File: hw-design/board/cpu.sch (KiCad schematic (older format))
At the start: 15 parts, among them P1 CONN_02X05, P2 CONN_02X05, U4 LPC1113FBD48/302, X1 10MHz

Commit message: sch: cpu reset done (wip)
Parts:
- removed R27, R28: 100R, Resistors_SMD:R_0603, symbol R
- added C? (x2): C, symbol C
- added C? (x3): 100nF X7R, Capacitors_SMD:C_0603, symbol C
- added C?: 10nF 500V, symbol C
- added C?: 10nF, symbol C
- added P?: USB_OTG, symbol USB_OTG
- added P?: CONN_01X04, symbol CONN_01X04
- added Q?: BC857, symbol Q_PNP_BEC
- added R? (x2): 33R, symbol R
- added R?: 100R, symbol R
- added R?: 1M, symbol R
- added R? (x2): 3k, symbol R
- added R?: 24k, symbol R
- added R? (x5): 10k, symbol R
- added SW?: SW_PUSH, symbol SW_PUSH
- added U?: LPC11U24FBD48/401, Housings_QFP:LQFP-80_12x12mm_Pitch0.5mm, symbol LPC11U24FBD48/401
- added Y?: 10MHz, symbol Crystal_Small
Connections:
- net +3V3: now also C?.2, C?.2, Q?.2 (E), R?.1, R?.1, R?.1, R?.1, R?.1, R?.2, U?.44 (VDD), U?.8 (VDD); no longer P2.1 (P1)
- net GNDD: now also C?.1, C?.1, C?.1, C?.2, C?.2, C?.2, C?.2, P?.1 (P1), P?.5 (GND), R?.1, SW?.2, U?.41 (VSS), U?.5 (VSS); no longer P2.7 (P7)
- net RESET: now also C?.2, R?.2, SW?.1, U?.3 (~RESET~/PIO0_0)
- net TCK_SWDCLK: now reaches P2.4 (P4)
- net TCK_SWDCLK: now also R?.2, U?.29 (SWCLK/PIO0_10/SCK0/CT16B0_MAT2)
- net TMS_SDWIO: now reaches P2.2 (P2)
- net TMS_SDWIO: now also R?.2, U?.33 (TMS/PIO0_12/AD1/CT32B1_CAP0)
- net TDO_SWO: now reaches P2.6 (P6)
- net TDO_SWO: now also R?.2, U?.34 (TDO/PIO0_13/AD2/CT32B1_MAT0)
- net TDI: now reaches P2.8 (P8)
- net TDI: now also R?.2, U?.32 (TDI/PIO0_11/AD0/CT32B0_MAT3)
- new net: C?.1, U?.6 (XTALIN), Y?.1
- new net: C?.1, U?.7 (XTALOUT), Y?.2
- new net: P?.2 (D-), R?.2
- new net: P?.3 (D+), R?.1, R?.2
- new net: C?.1, P?.6 (shield), R?.2
- new net: Q?.1 (B), R?.1, R?.2
- new net: Q?.3 (C), R?.2
- new net CHAIN_DE: P?.4 (P4), U?.43 (PIO1_15/~DCD~/CT16B0_MAT2/SCK1)
- new net CHAIN_RX: P?.3 (P3), U?.37 (PIO1_14/~DSR~/CT16B0_MAT1/RXD)
- new net CHAIN_TX: P?.2 (P2), U?.36 (PIO1_13/~DTR~/CT16B0_MAT0/TXD)
- new net USB_CONNECT: R?.1, U?.22 (PIO0_6/~USB_CONNECT~/SCK0)
- new net USB_DM: R?.1, U?.19 (USB_DM)
- new net USB_DP: R?.1, U?.20 (USB_DP)
- new net USB_VBUS: R?.1, U?.14 (PIO0_3/USB_VBUS)
- new net VCC: C?.1, P?.1 (VCC), R?.2
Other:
- note added: "JTAG"
- note added: "RESET"
- note added: "USB DEVICE"
- note removed: "SWD"
- moved on the sheet: C12, C13, C14, C15, C16, P1, P2, R23, R24, R25, R26, U4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

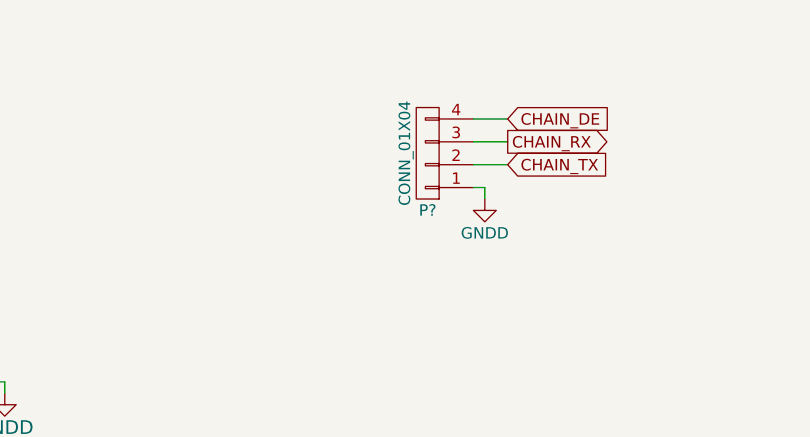
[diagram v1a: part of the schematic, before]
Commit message: sch: cpu, I/Os and control chain circuits done
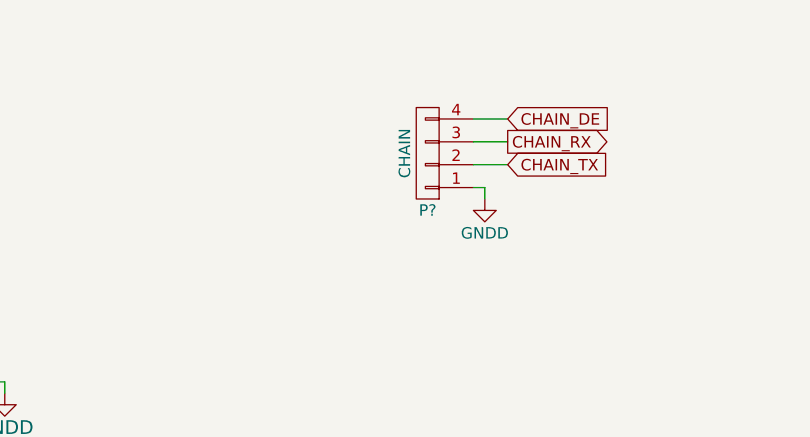
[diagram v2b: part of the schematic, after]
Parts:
- P?: value CONN_01X04 -> CHAIN
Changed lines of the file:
@@
 P 1450 1250
 F 0 "P?" H 1450 1500 50  0000 C CNN
-F 1 "CONN_01X04" V 1550 1250 50  0000 C CNN
+F 1 "CHAIN" V 1550 1250 50  0000 C CNN
 F 2 "" H 1450 1250 60  0000 C CNN
 F 3 "" H 1450 1250 60  0000 C CNN

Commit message: sch: schematic annotation done
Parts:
- removed C12, C14: 18pF X7R, Capacitors_SMD:C_0603, symbol C
- removed C13, C15, C16: 100nF X7R, Capacitors_SMD:C_0603, symbol C
- removed P1: CONN_02X05, Pin_Headers:Pin_Header_Straight_2x05, symbol CONN_02X05
- removed R23: 10k, Resistors_SMD:R_0603, symbol R
- removed R24, R25, R26: 0R, Resistors_SMD:R_0603, symbol R
- removed R? (x4): 10k, symbol R
- removed U4: LPC1113FBD48/302, Housings_QFP:LQFP-48_7x7mm_Pitch0.5mm, symbol LPC1113FBD48/302
- removed X1: 10MHz, Crystals_Oscillators_SMD:Q_49U3HMS, symbol Crystal
- gave numbers to parts that had none: 21
- renumbered P2 to P3
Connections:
- net POT: now also U4.32 (TDI/PIO0_11/AD0/CT32B0_MAT3)
- net SWDIO: now also U4.39 (SWDIO/PIO0_15/AD4/CT32B1_MAT2)
- net CH2: now reaches U4.13 (PIO1_20/~DSR~/SCK1)
- net FS1: now reaches U4.18 (PIO1_23/CT16B1_MAT1/SSEL1)
- net CH1: now reaches U4.2 (PIO1_19/~DTR~/SSEL1)
- net FS1_LED_R: now reaches U4.24 (PIO1_28/CT32B0_CAP0/SCLK)
- net FS1_LED_B: now reaches U4.25 (PIO1_31)
- net CH3: now reaches U4.26 (PIO1_21/~DCD~/MISO1)
- net SWO: now reaches U4.28 (PIO0_9/MOSI0/CT16B0_MAT1)
- net SWO: now also P3.6 (P6)
- net FS1_LED_G: now reaches U4.31 (PIO1_29/SCK0/CT32B0_CAP1)
- net RS485_RX_LED: now reaches U4.46 (PIO0_18/RXD/CT32B0_MAT0)
- net RS485_TX_LED: now reaches U4.47 (PIO0_19/TXD/CT32B0_MAT1)
- net TCK_SWDCLK renamed SWCLK
- net TDI: no longer names the net of P3.8 (P8)
- net TDI: no longer U4.32 (TDI/PIO0_11/AD0/CT32B0_MAT3)
- net TDO_SWO: no longer names the net of U4.34 (TDO/PIO0_13/AD2/CT32B1_MAT0)
- net TDO_SWO: no longer P3.6 (P6)
- net TMS_SDWIO: no longer names the net of U4.33 (TMS/PIO0_12/AD1/CT32B1_CAP0)
- net TMS_SDWIO: no longer P3.2 (P2)
- new net SDWIO: P3.2 (P2)
- no-connect marks 33 -> 24
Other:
- note added: "SWD"
- note removed: "JTAG"
- moved on the sheet: C16, P3, R21, SW1

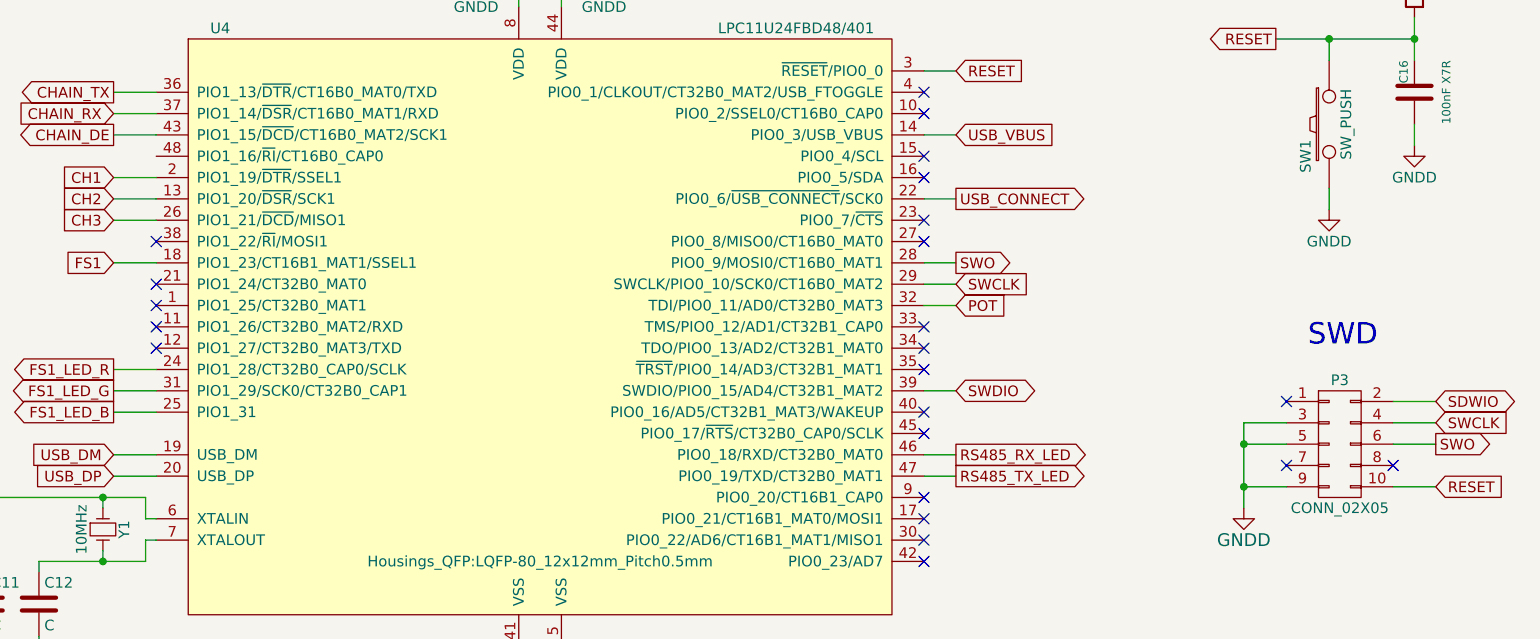
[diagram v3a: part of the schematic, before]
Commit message: sch: errors fixed, DRC passing
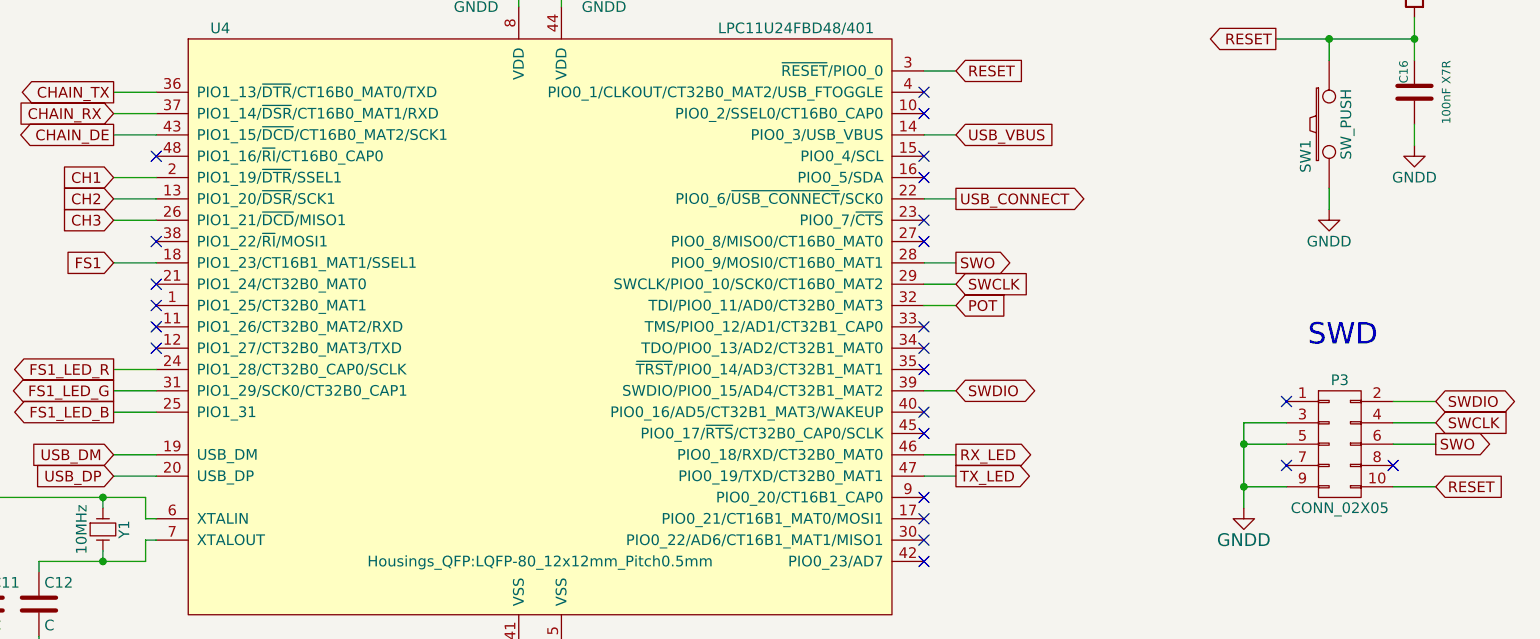
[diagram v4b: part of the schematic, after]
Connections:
- net SDWIO is gone; now on net SWDIO: P3.2 (P2)
- net RS485_RX_LED renamed RX_LED
- net RS485_TX_LED renamed TX_LED
- no-connect marks 24 -> 25
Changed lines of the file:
@@
 SWD
 $Comp
-L GNDD #PWR040
+L GNDD #PWR043
 U 1 1 54E5DFA7
 P 9200 3950
-F 0 "#PWR040" H 9200 3700 60  0001 C CNN
+F 0 "#PWR043" H 9200 3700 60  0001 C CNN
 F 1 "GNDD" H 9200 3800 60  0000 C CNN
 F 2 "" H 9200 3950 60  0000 C CNN
@@
 $EndComp
 $Comp
-L GNDD #PWR041
+L GNDD #PWR044
 U 1 1 556F6417
 P 3300 4600
-F 0 "#PWR041" H 3300 4350 50  0001 C CNN
+F 0 "#PWR044" H 3300 4350 50  0001 C CNN
 F 1 "GNDD" H 3300 4450 50  0000 C CNN
 F 2 "" H 3300 4600 60  0000 C CNN
@@
 $EndComp
 $Comp
-L GNDD #PWR042
+L GNDD #PWR045
 U 1 1 556F65EC
 P 3550 4600
-F 0 "#PWR042" H 3550 4350 50  0001 C CNN
+F 0 "#PWR045" H 3550 4350 50  0001 C CNN
 F 1 "GNDD" H 3550 4450 50  0000 C CNN
 F 2 "" H 3550 4600 60  0000 C CNN
@@
 USB_VBUS
 $Comp
-L +3.3V #PWR043
+L +3.3V #PWR046
 U 1 1 55705A80
 P 5900 850
-F 0 "#PWR043" H 5900 700 50  0001 C CNN
+F 0 "#PWR046" H 5900 700 50  0001 C CNN
 F 1 "+3.3V" H 5900 990 50  0000 C CNN
 F 2 "" H 5900 850 60  0000 C CNN
@@
 $EndComp
 $Comp
-L GNDD #PWR044
+L GNDD #PWR047
 U 1 1 557DC875
 P 5600 1450
-F 0 "#PWR044" H 5600 1200 50  0001 C CNN
+F 0 "#PWR047" H 5600 1200 50  0001 C CNN
 F 1 "GNDD" H 5600 1300 50  0000 C CNN
 F 2 "" H 5600 1450 60  0000 C CNN
@@
 $EndComp
 $Comp
-L GNDD #PWR045
+L GNDD #PWR048
 U 1 1 557DCAD9
 P 6200 1450
-F 0 "#PWR045" H 6200 1200 50  0001 C CNN
+F 0 "#PWR048" H 6200 1200 50  0001 C CNN
 F 1 "GNDD" H 6200 1300 50  0000 C CNN
 F 2 "" H 6200 1450 60  0000 C CNN
@@
 $EndComp
 $Comp
-L GNDD #PWR046
+L GNDD #PWR049
 U 1 1 557DD01E
 P 5900 4750
-F 0 "#PWR046" H 5900 4500 50  0001 C CNN
+F 0 "#PWR049" H 5900 4500 50  0001 C CNN
 F 1 "GNDD" H 5900 4600 50  0000 C CNN
 F 2 "" H 5900 4750 60  0000 C CNN
@@
 $EndComp
 $Comp
-L GNDD #PWR047
+L GNDD #PWR050
 U 1 1 557DE7E3
 P 2850 6600
-F 0 "#PWR047" H 2850 6350 50  0001 C CNN
+F 0 "#PWR050" H 2850 6350 50  0001 C CNN
 F 1 "GNDD" H 2850 6450 50  0000 C CNN
 F 2 "" H 2850 6600 60  0000 C CNN
@@
 $EndComp
 $Comp
-L VCC #PWR048
+L VCC #PWR051
 U 1 1 557DE7F0
 P 3750 6300
-F 0 "#PWR048" H 3750 6150 50  0001 C CNN
+F 0 "#PWR051" H 3750 6150 50  0001 C CNN
 F 1 "VCC" H 3750 6450 50  0000 C CNN
 F 2 "" H 3750 6300 60  0000 C CNN
@@
 $EndComp
 $Comp
-L +3.3V #PWR049
+L +3.3V #PWR052
 U 1 1 557E22DB
 P 2050 6500
-F 0 "#PWR049" H 2050 6350 50  0001 C CNN
+F 0 "#PWR052" H 2050 6350 50  0001 C CNN
 F 1 "+3.3V" H 2050 6640 50  0000 C CNN
 F 2 "" H 2050 6500 60  0000 C CNN
@@
 $EndComp
 $Comp
-L GNDD #PWR050
+L GNDD #PWR053
 U 1 1 557EA320
 P 3750 6900
-F 0 "#PWR050" H 3750 6650 50  0001 C CNN
+F 0 "#PWR053" H 3750 6650 50  0001 C CNN
 F 1 "GNDD" H 3750 6750 50  0000 C CNN
 F 2 "" H 3750 6900 60  0000 C CNN
@@
 $EndComp
 $Comp
-L GNDD #PWR051
+L GNDD #PWR054
 U 1 1 557F3440
 P 1700 1450
-F 0 "#PWR051" H 1700 1200 50  0001 C CNN
+F 0 "#PWR054" H 1700 1200 50  0001 C CNN
 F 1 "GNDD" H 1700 1300 50  0000 C CNN
 F 2 "" H 1700 1450 60  0000 C CNN
@@
 	9900 3550 10100 3550
 Text GLabel 10100 3450 2    50   BiDi ~ 0
-SDWIO
+SWDIO
 Wire Wire Line
 	9900 3450 10100 3450
@@
 	7850 1900 7700 1900
 $Comp
-L +3.3V #PWR052
+L +3.3V #PWR055
 U 1 1 55802FA1
 P 10000 1250
-F 0 "#PWR052" H 10000 1100 50  0001 C CNN
+F 0 "#PWR055" H 10000 1100 50  0001 C CNN
 F 1 "+3.3V" H 10000 1390 50  0000 C CNN
 F 2 "" H 10000 1250 60  0000 C CNN
@@
 	10000 1350 10000 1250
 $Comp
-L GNDD #PWR053
+L GNDD #PWR056
 U 1 1 55803C49
 P 10000 2250
-F 0 "#PWR053" H 10000 2000 50  0001 C CNN
+F 0 "#PWR056" H 10000 2000 50  0001 C CNN
 F 1 "GNDD" H 10000 2100 50  0000 C CNN
 F 2 "" H 10000 2250 60  0000 C CNN
@@
 Connection ~ 9600 1750
 $Comp
-L GNDD #PWR054
+L GNDD #PWR057
 U 1 1 55806665
 P 9600 2550
-F 0 "#PWR054" H 9600 2300 50  0001 C CNN
+F 0 "#PWR057" H 9600 2300 50  0001 C CNN
 F 1 "GNDD" H 9600 2400 50  0000 C CNN
 F 2 "" H 9600 2550 60  0000 C CNN
@@
 	4100 2800 3900 2800
 Text GLabel 7850 3700 2    50   Output ~ 0
-RS485_RX_LED
+RX_LED
 Wire Wire Line
 	7850 3700 7700 3700
 Text GLabel 7850 3800 2    50   Output ~ 0
-RS485_TX_LED
+TX_LED
 Wire Wire Line
 	7850 3800 7700 3800
@@
 NoConn ~ 7700 4100
 NoConn ~ 7700 4200
+NoConn ~ 4100 2300
 $EndSCHEMATC

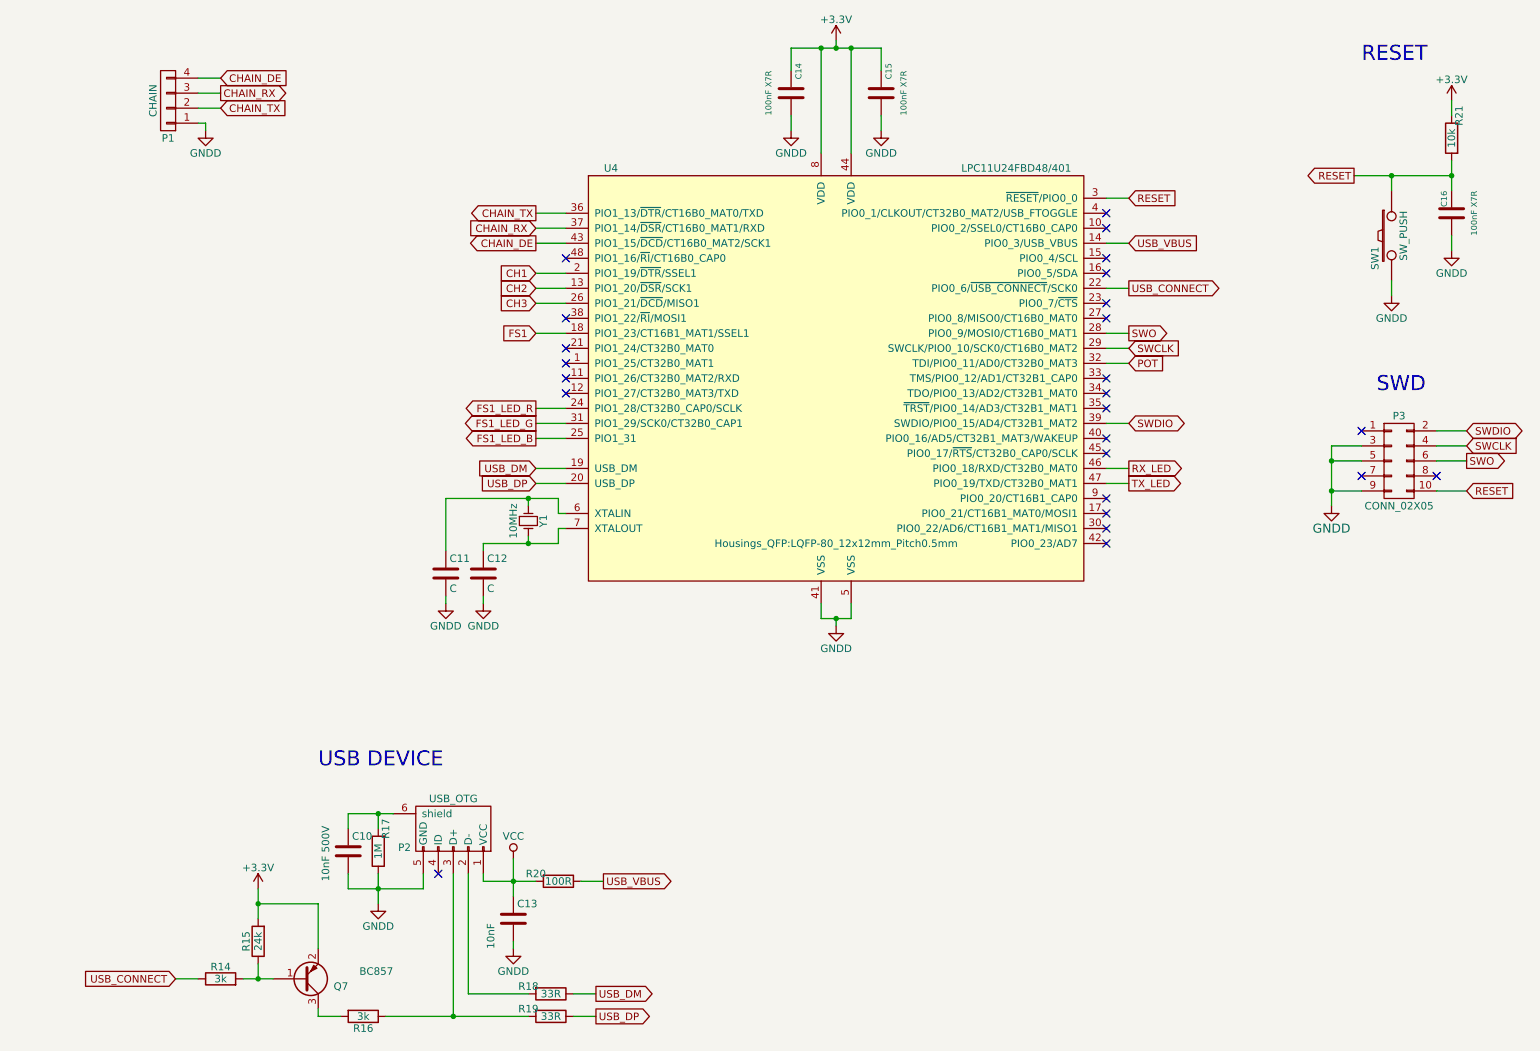
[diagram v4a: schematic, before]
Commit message: sch: adding values and MPN to components
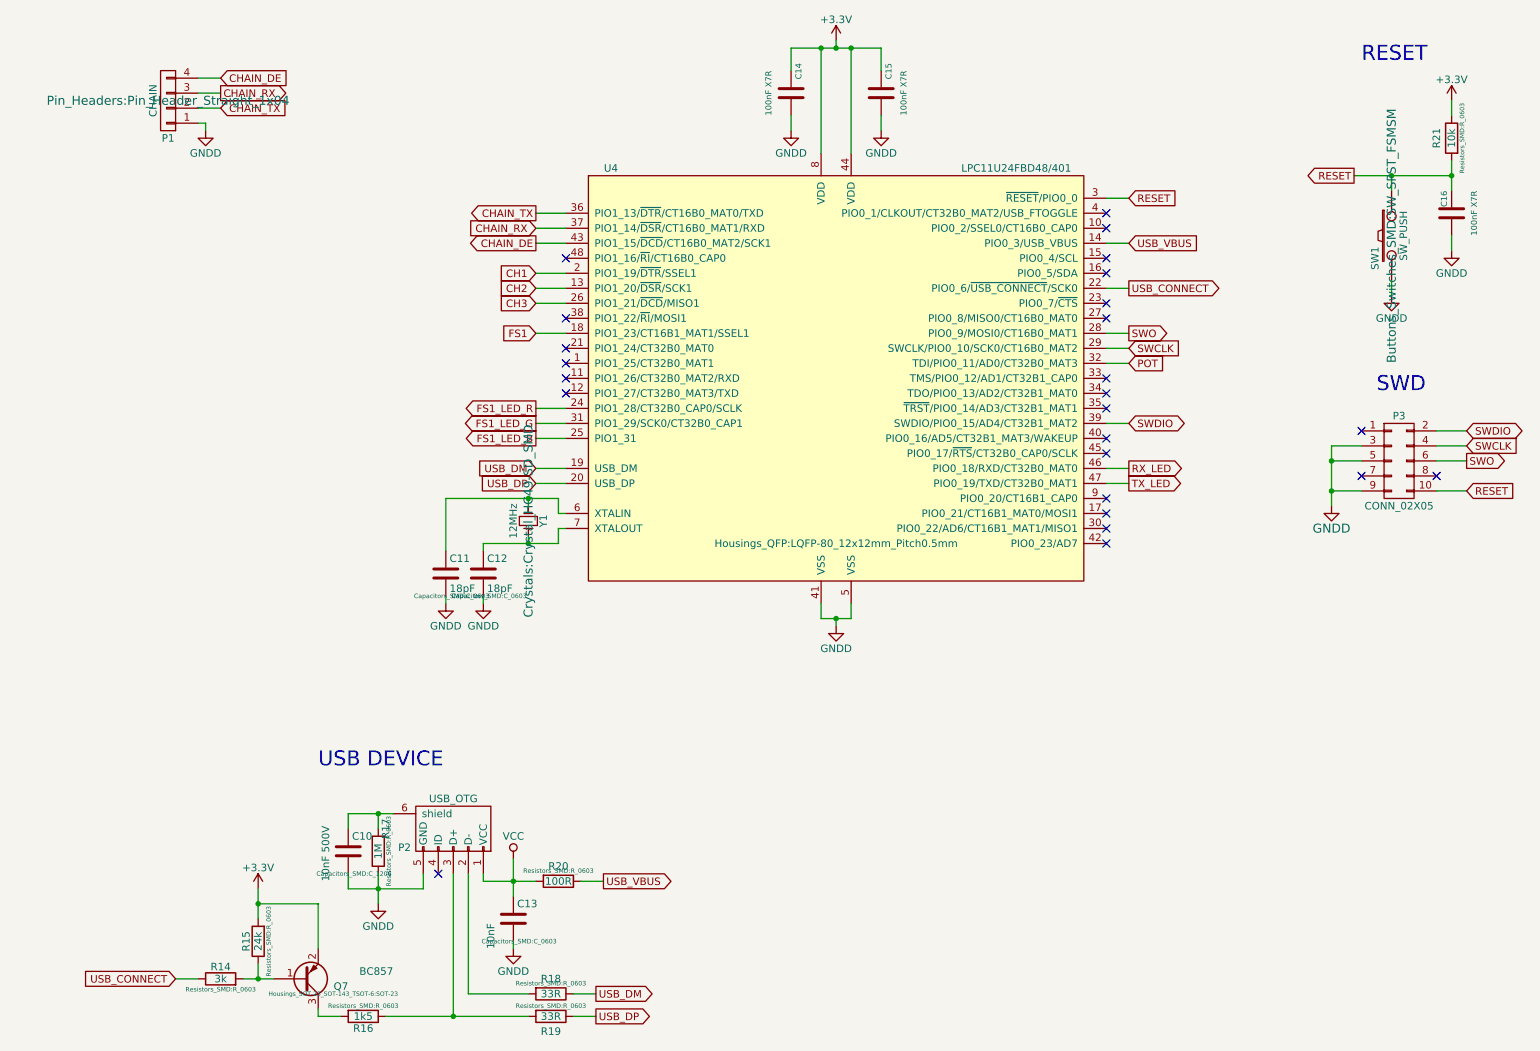
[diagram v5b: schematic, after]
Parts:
- C10: footprint (none) -> Capacitors_SMD:C_1206; MPN (none) -> 501R18W103KV4E
- C11, C12: value C -> 18pF; footprint (none) -> Capacitors_SMD:C_0603; MPN (none) -> C1608C0G1H180J080AA
- C13: footprint (none) -> Capacitors_SMD:C_0603; MPN (none) -> C1608X7R1E103K080AA
- C14, C15, C16: MPN (none) -> C1608X7R1E104K080AA
- P1: footprint (none) -> Pin_Headers:Pin_Header_Straight_1x04; MPN (none) -> -
- P2: MPN (none) -> 10033526-N3212LF
- P3: MPN (none) -> -
- Q7: footprint (none) -> Housings_SOT-23_SOT-143_TSOT-6:SOT-23; MPN (none) -> BC857B,215
- R14: footprint (none) -> Resistors_SMD:R_0603; MPN (none) -> MCR03ERTF3001
- R15: footprint (none) -> Resistors_SMD:R_0603; MPN (none) -> MCR03ERTF2402
- R16: value 3k -> 1k5; footprint (none) -> Resistors_SMD:R_0603; MPN (none) -> MCR03ERTF1501
- R17: footprint (none) -> Resistors_SMD:R_0603; MPN (none) -> RMCF0603JT1M00
- R18, R19: footprint (none) -> Resistors_SMD:R_0603; MPN (none) -> MCR03ERTF33R0
- R20: footprint (none) -> Resistors_SMD:R_0603; MPN (none) -> RMCF0603JT100R
- R21: footprint (none) -> Resistors_SMD:R_0603; MPN (none) -> RMCF0603JT10K0
- SW1: footprint (none) -> Buttons_Switches_SMD:SW_SPST_FSMSM; MPN (none) -> FSMSM
- U4: MPN (none) -> LPC11U24FBD48/401
- Y1: value 10MHz -> 12MHz; footprint (none) -> Crystals:Crystal_HC49-SD_SMD; MPN (none) -> FOXSDLF/120-20

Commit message: sch: JTAG connector footprint fixed
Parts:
- P3: footprint Pin_Headers:Pin_Header_Straight_2x05 -> Pin_Headers:Pin_Header_Straight_2x05_Pitch1.27mm
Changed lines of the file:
@@
 F 0 "P3" H 9650 3950 50  0000 C CNN
 F 1 "CONN_02X05" H 9650 3350 50  0000 C CNN
-F 2 "Pin_Headers:Pin_Header_Straight_2x05" H 9650 2450 60  0001 C CNN
+F 2 "Pin_Headers:Pin_Header_Straight_2x05_Pitch1.27mm" H 9650 2450 60  0001 C CNN
 F 3 "" H 9650 2450 60  0000 C CNN
 F 4 "-" H 0   0   50  0001 C CNN "MPN"
